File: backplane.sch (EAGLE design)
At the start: 55 parts, among them J1 L717HDE15PD4CH4R, J10 5013310807, J11 5013310807, J12 5013310807, J13 5013310807, J14 5013311007, J15 5013311007, J16 5013311007, J17 5013311007, J18 5013311007, J19 5013311007, J2 1054301102, J20 5013311007, J21 5013311007, J22 5013311007, J23 5013311007, J24 SEAM-40-03.0-S-06-2-A-K-TR, J25 5055670271, J3 5011902017, J4 5013310807, J5 5013310807, J6 5013310807, J7 5013310807, J8 5013310807, J9 5013310807, U1 AM26LV32EIPWR, U10 AM26LV32EIPWR, U2 AM26LV32EIPWR, U3 AM26LV32EIPWR, U4 AM26LV32EIPWR, U5 AM26LV32EIPWR, U6 AM26LV32EIPWR, U7 AM26LV32EIPWR, U8 AM26LV32EIPWR, U9 AM26LV32EIPWR

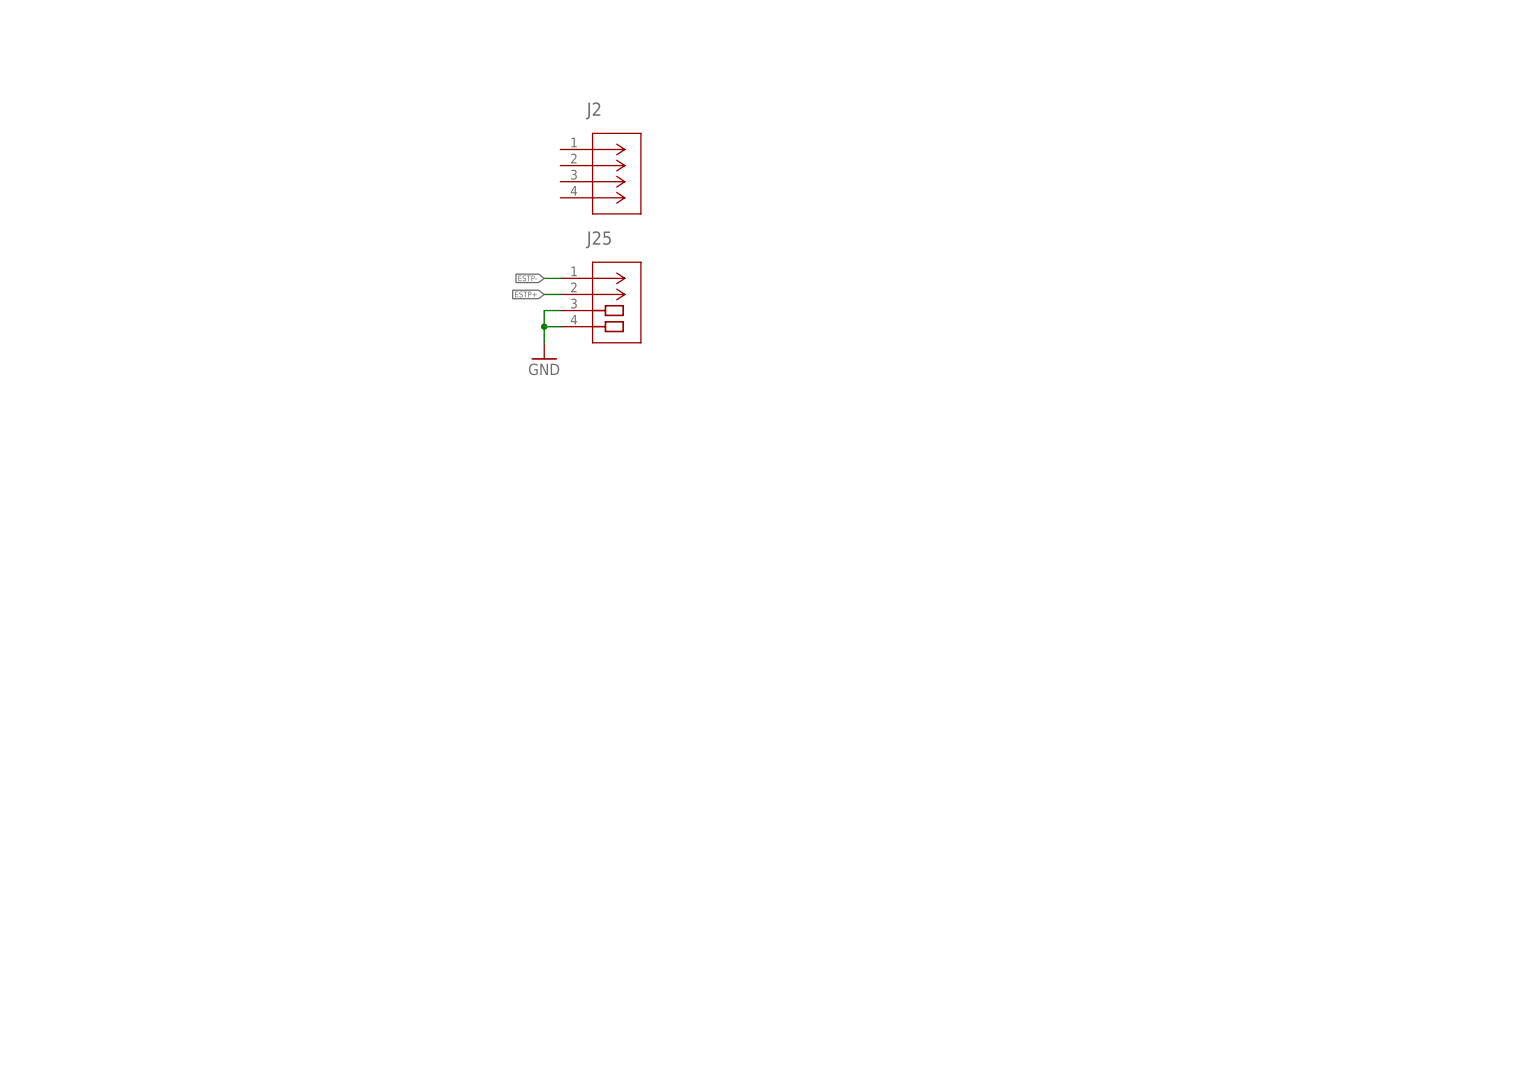
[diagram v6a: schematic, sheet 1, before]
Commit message: added filter, 3v3 reg, and extra DIO
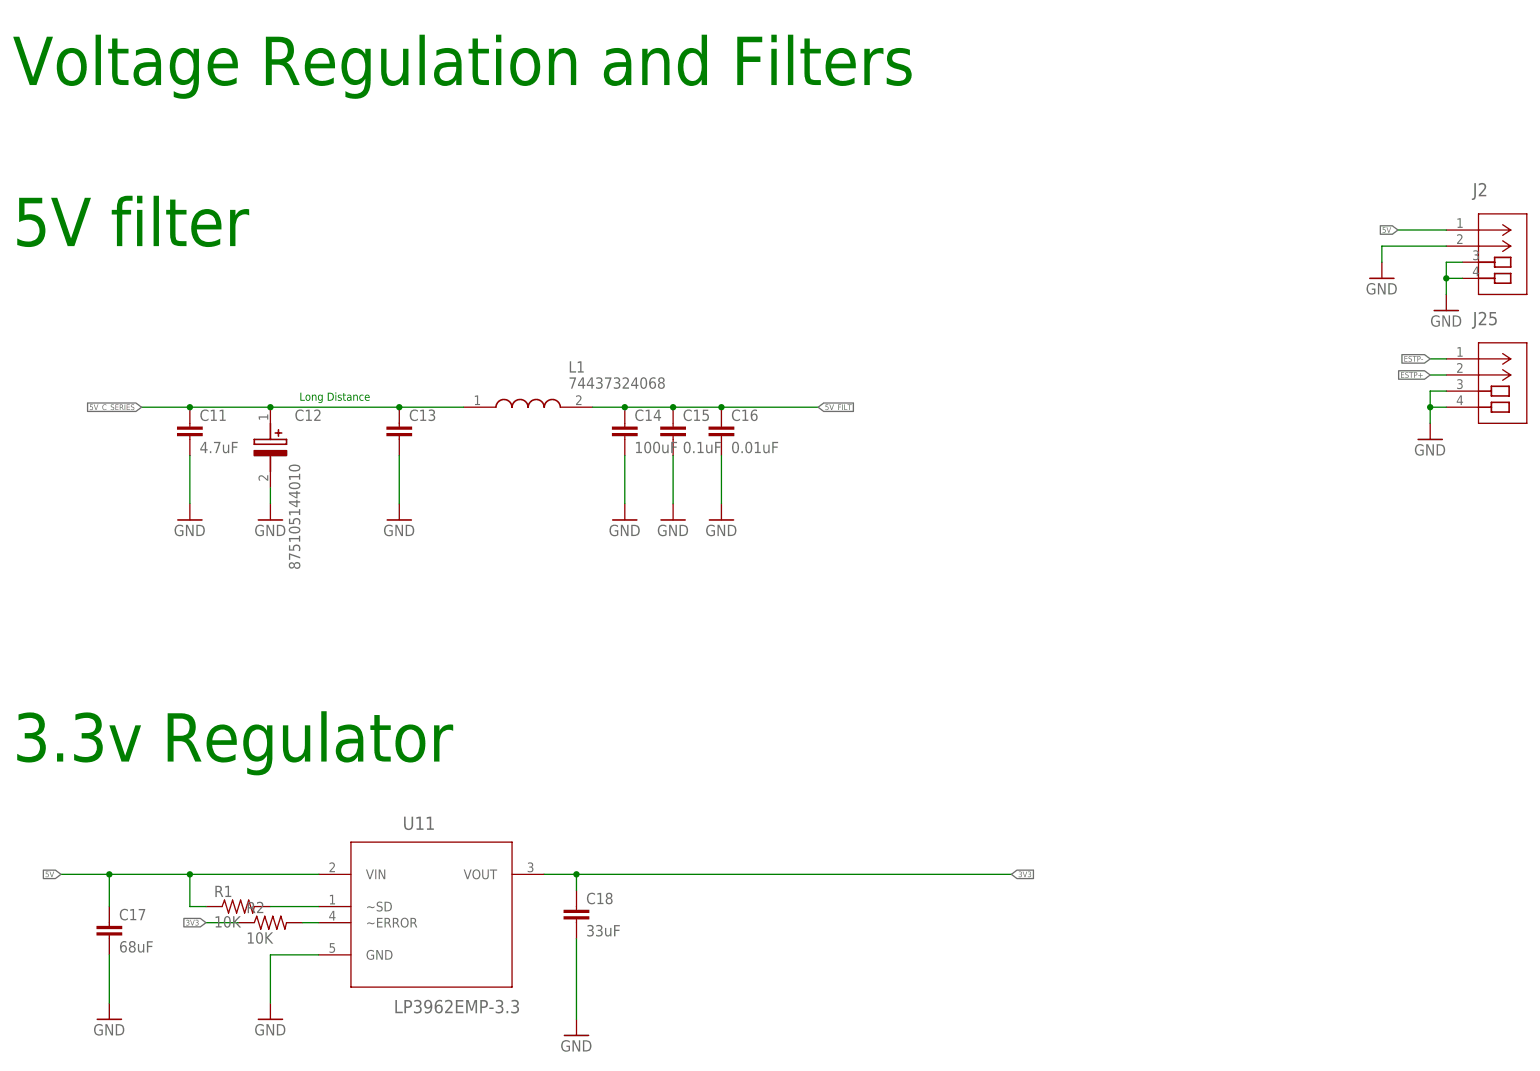
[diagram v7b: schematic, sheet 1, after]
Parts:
- added C11: 4.7uF, rcl:C-EUC0603
- added C12: 875105144010, sbrio_backplane:875105144010
- added C13: (no value), rcl:C-EUC0603
- added C14: 100uF, rcl:C-EUC1206
- added C15: 0.1uF, rcl:C-EUC0603
- added C16: 0.01uF, rcl:C-EUC0603
- added C17: 68uF, rcl:C-EUC1206
- added C18: 33uF, rcl:C-EUC1206
- added J26, J27, J28, J29: SAMTEC-TST-110-01-X-DJ, sbrio_backplane:SAMTEC-TST-110-01-X-DJ
- added L1: 74437324068, sbrio_backplane:74437324068
- added R1, R2: 10K, rcl:R-US_R0603
- added U11: LP3962EMP-3.3, sbrio_backplane:LP3962EMP-3.3
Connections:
- new net 3V3_SBRIO: J24G$3.F8, J26.1
- new net 5V_SBRIO: J24G$3.F10, J24G$3.F11, J24G$3.F12, J24G$3.F9, J26.3, J26.5
- new net DIO18: J24G$2.C36
- new net DIO19: J24G$2.C35
- new net DIO20: J24G$2.C33
- new net DIO21: J24G$2.C32, J29.15
- new net DIO22: J24G$2.C30, J29.7
- new net DIO23: J24G$2.C29, J29.3
- new net DIO24: J24G$2.C27, J28.15
- new net DIO25: J24G$2.C26, J28.11
- new net DIO26: J24G$2.C24, J28.3
- new net DIO27: J24G$2.C23, J27.19
- new net DIO28: J24G$2.C21, J27.11
- new net DIO29: J24G$2.C20, J27.7
- new net DIO30: J24G$2.C18, J26.15
- new net DIO31: J24G$2.C17, J26.11
- new net DIO50: J24G$1.B36
- new net DIO51: J24G$1.B34
- new net DIO52: J24G$1.B33, J29.17
- new net DIO53: J24G$1.B31, J29.11
- new net DIO54: J24G$1.B30, J29.5
- new net DIO55: J24G$1.B28, J28.19
- new net DIO56: J24G$1.B27, J28.13
- new net DIO57: J24G$1.B25, J28.7
- new net DIO58: J24G$1.B24, J28.1
- new net DIO59: J24G$1.B22, J27.15
- new net DIO60: J24G$1.B21, J27.9
- new net DIO61: J24G$1.B19, J27.3
- new net DIO62: J24G$1.B18, J26.17
- new net DIO85: J24G$1.A32, J29.13
- new net DIO86: J24G$1.A31, J29.9
- new net DIO87: J24G$1.A29, J29.1
- new net DIO88: J24G$1.A28, J28.17
- new net DIO89: J24G$1.A26, J28.9
- new net DIO90: J24G$1.A25, J28.5
- new net DIO91: J24G$1.A23, J27.17
- new net DIO92: J24G$1.A22, J27.13
- new net DIO93: J24G$1.A20, J27.5
- new net DIO94: J24G$1.A19, J27.1
- new net DIO95: J24G$1.A17, J26.13
- new net N$1: R1.2, U11.~SD
- new net N$15: J24G$1.B16
- new net N$2: R2.2, U11.~ERROR
- net 3V3: now also C18.1, R2.1, U11.VOUT
- net 5V: now also C17.1, J2.1, R1.1, U11.VIN
- net 5V_C_SERIES: now also C11.1, C12.+, C13.1, J29.19, L1.1
- net 5V_FILT: now also C14.1, C15.1, C16.1, L1.2
- net DIO77: now also J26.19
- net DIO78: now also J26.9
- net DIO79: now also J26.7
- net GND: now also C11.2, C12.-, C13.2, C14.2, C15.2, C16.2, C17.2, C18.2, J2.2, J2.3, J2.4, J26.10, J26.12, J26.14, J26.16, J26.18, J26.2, J26.20, J26.4, J26.6, J26.8, J27.10, J27.12, J27.14, J27.16, J27.18, J27.2, J27.20, J27.4, J27.6, J27.8, J28.10, J28.12, J28.14, J28.16, J28.18, J28.2, J28.20, J28.4, J28.6, J28.8, J29.10, J29.12, J29.14, J29.16, J29.18, J29.2, J29.20, J29.4, J29.6, J29.8, U11.GND
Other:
- note added: "3.3v Regulator"
- note added: "5V filter"
- note added: "Long Distance"
- note added: "Voltage Regulation and Filters"
- moved on the sheet: J25

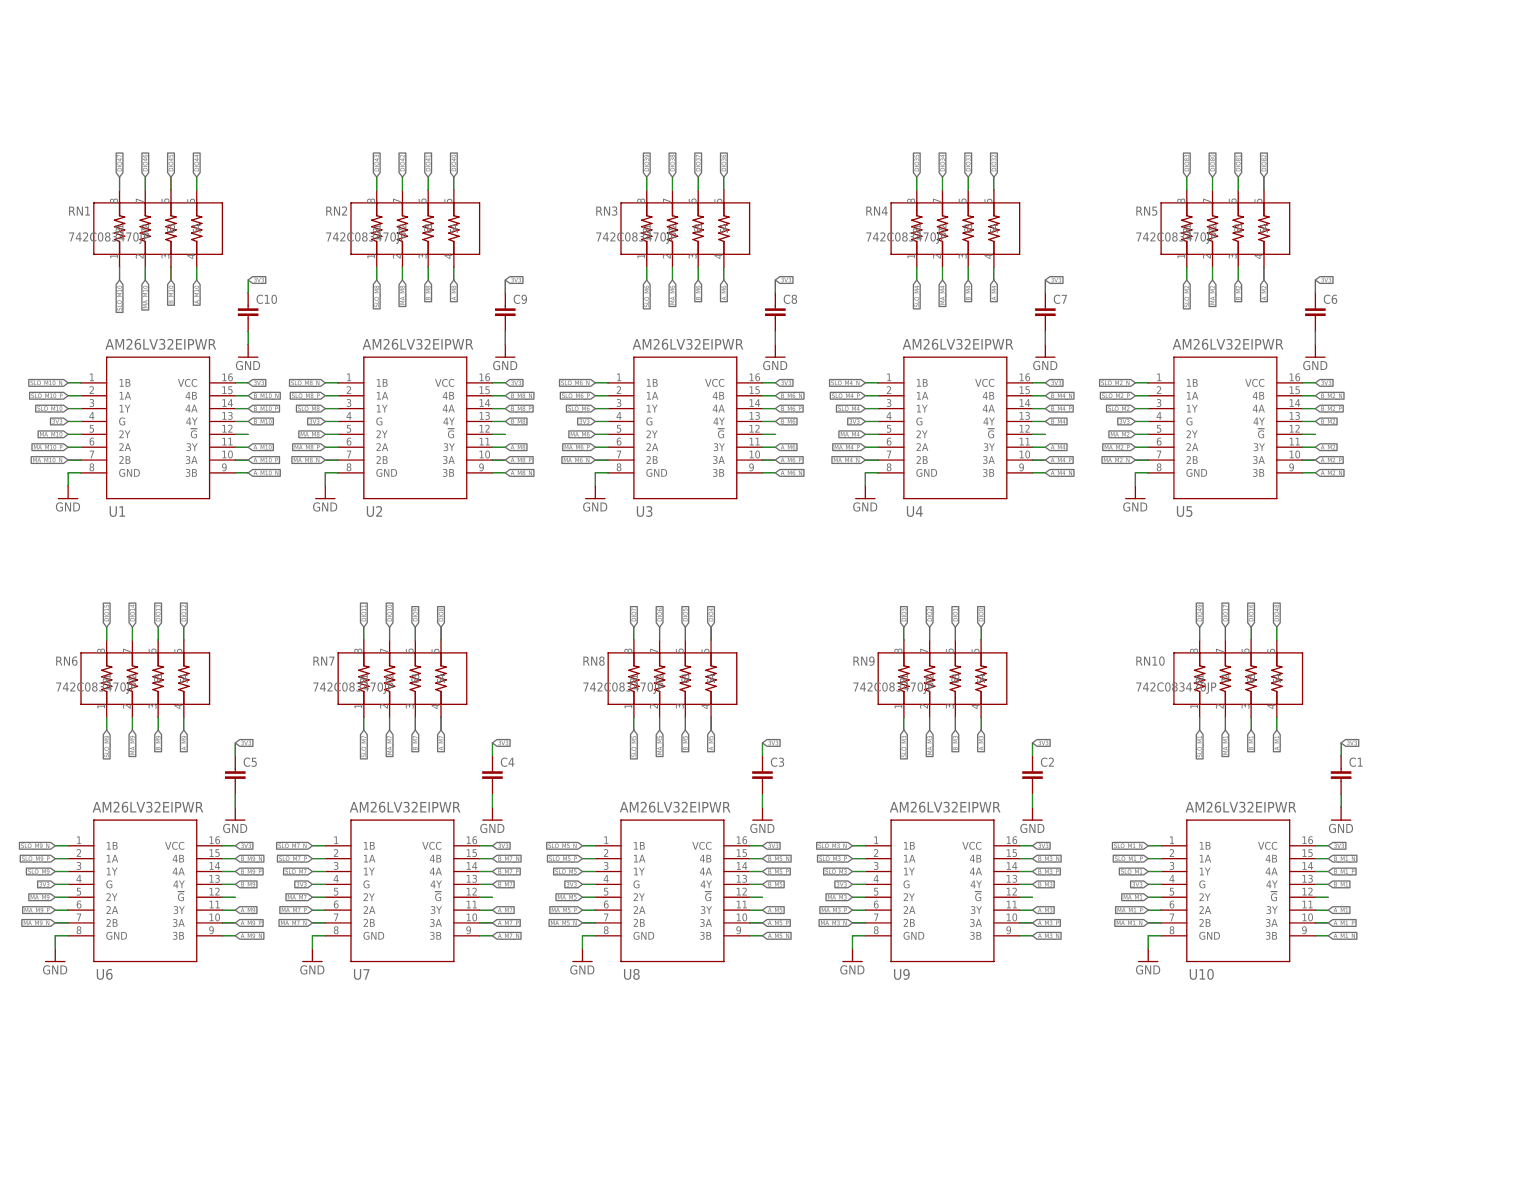
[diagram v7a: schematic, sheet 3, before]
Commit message: DRC Checks passed, in-depth review INCOMPLETE
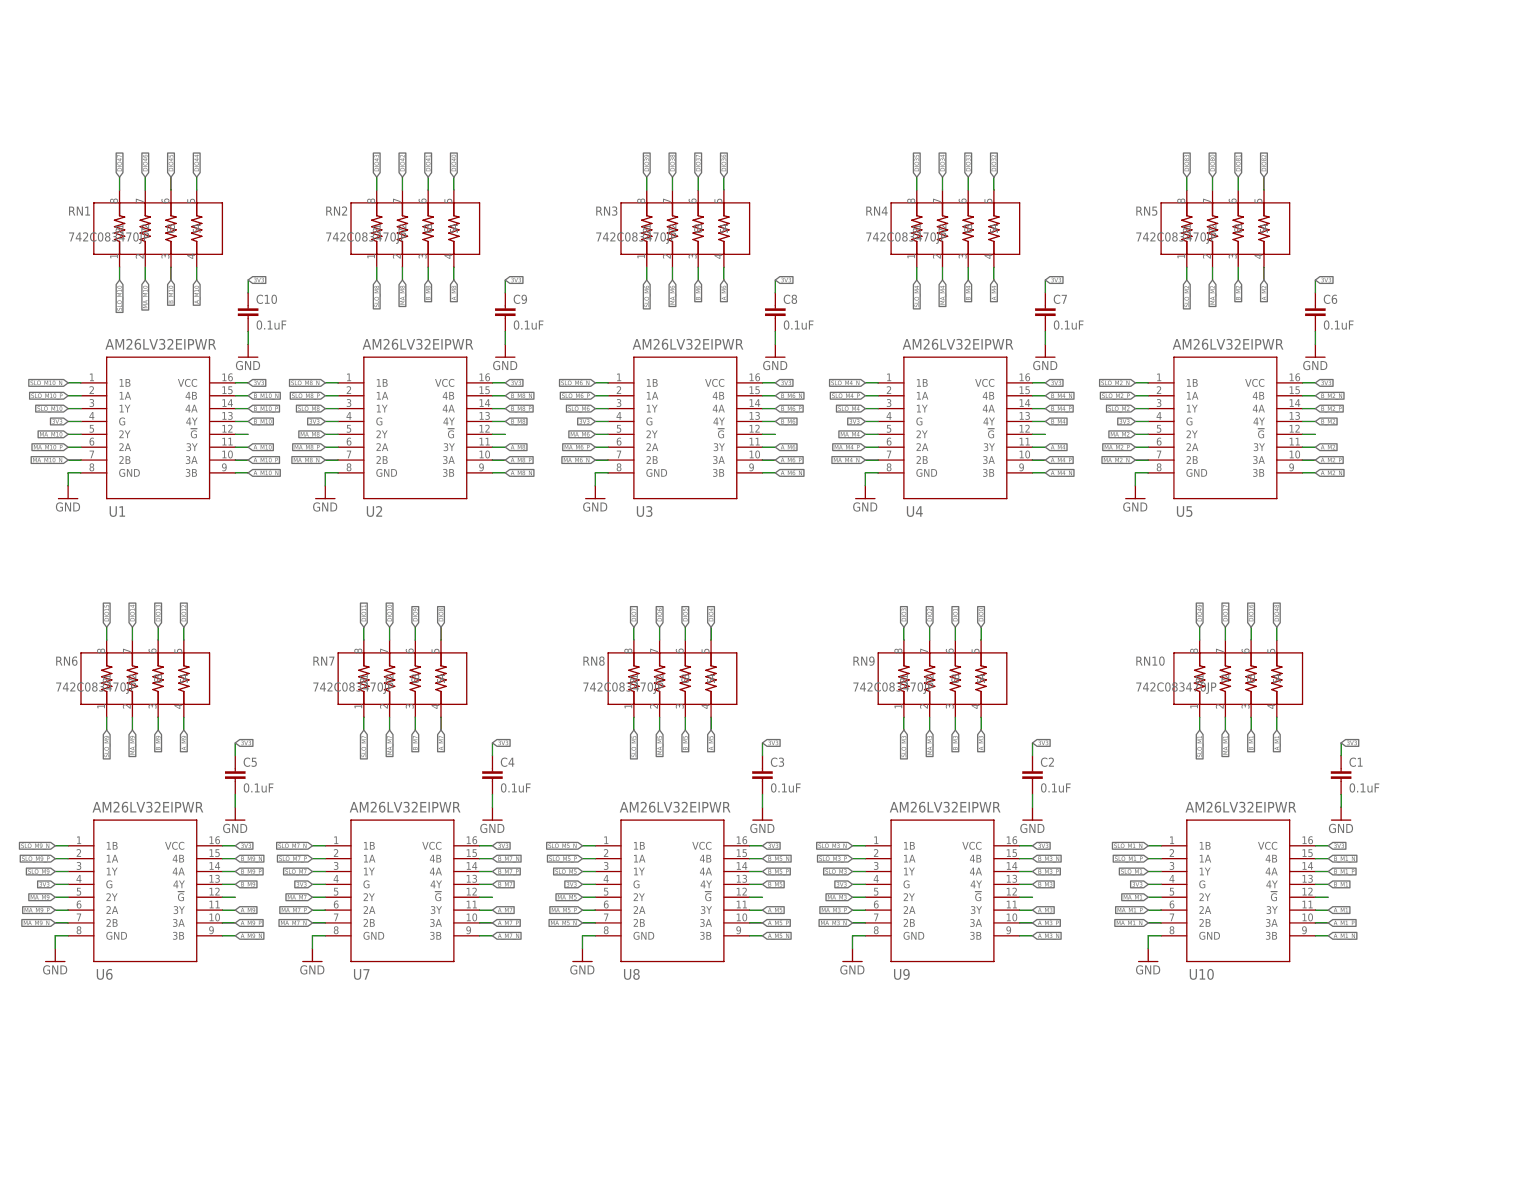
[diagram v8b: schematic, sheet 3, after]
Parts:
- C1, C10, C2, C3, C4, C5, C6, C7, C8, C9: value (none) -> 0.1uF
